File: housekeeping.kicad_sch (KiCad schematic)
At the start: 41 parts, among them U14 MC34063A, U15 MC34063A, U16 TPS54302

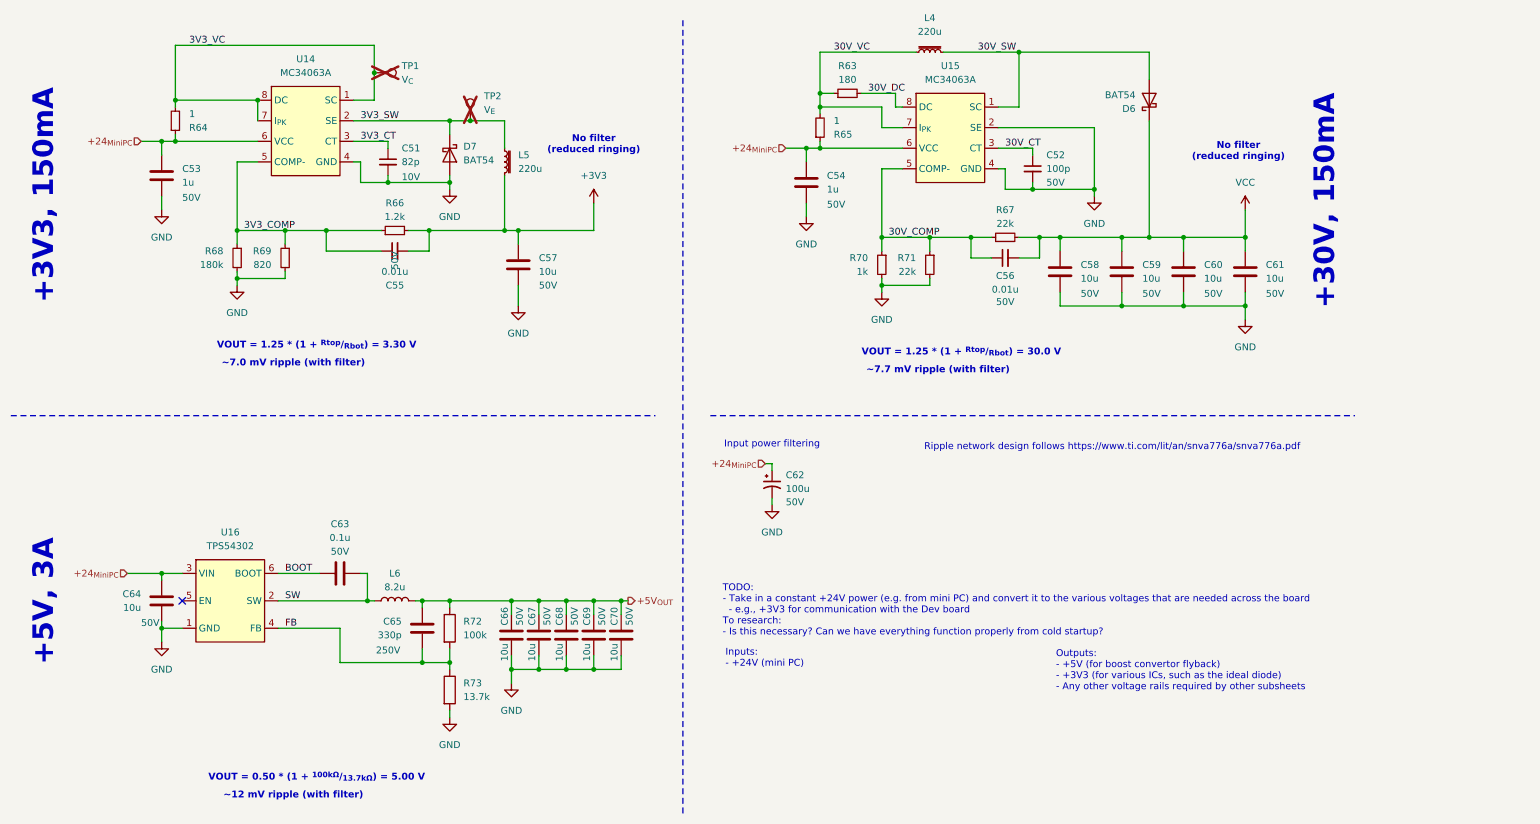
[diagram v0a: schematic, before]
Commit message: Add test points to all subsheets
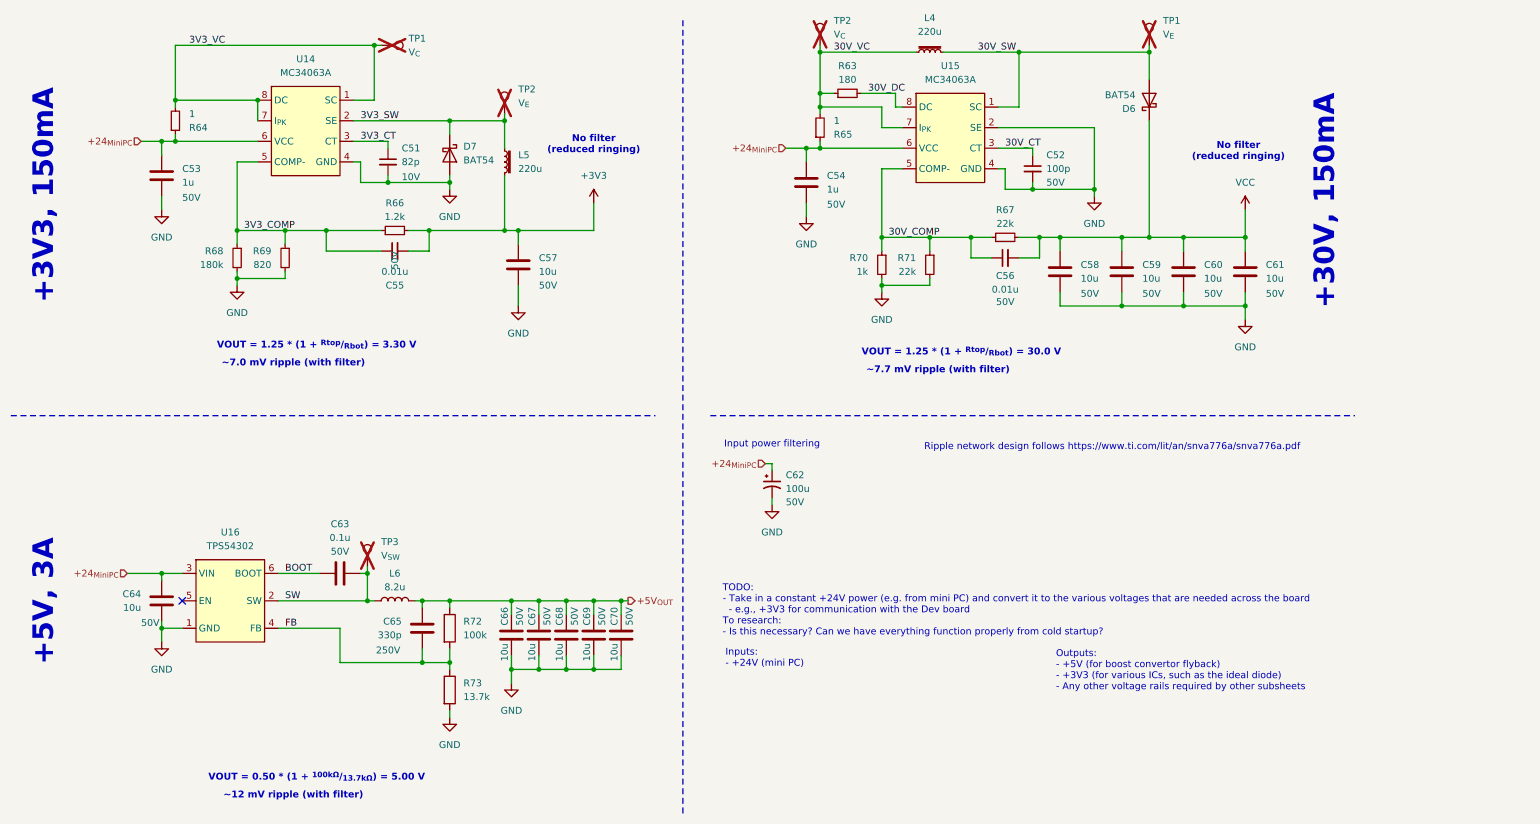
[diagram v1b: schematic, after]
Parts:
- added TP1: V_{E}, TestPoint:TestPoint_Bridge_Pitch2.0mm_Drill0.7mm, symbol Connector:TestPoint
- added TP2: V_{C}, TestPoint:TestPoint_Bridge_Pitch2.0mm_Drill0.7mm, symbol Connector:TestPoint
- added TP3: V_{SW}, TestPoint:TestPoint_Bridge_Pitch2.0mm_Drill0.7mm, symbol Connector:TestPoint
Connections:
- net 30V_SW: now also TP1.1
- net 30V_VC: now also TP2.1
- net SW: now also TP3.1
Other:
- moved on the sheet: TP1, TP2

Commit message: Renumbered components for rev 1b layout
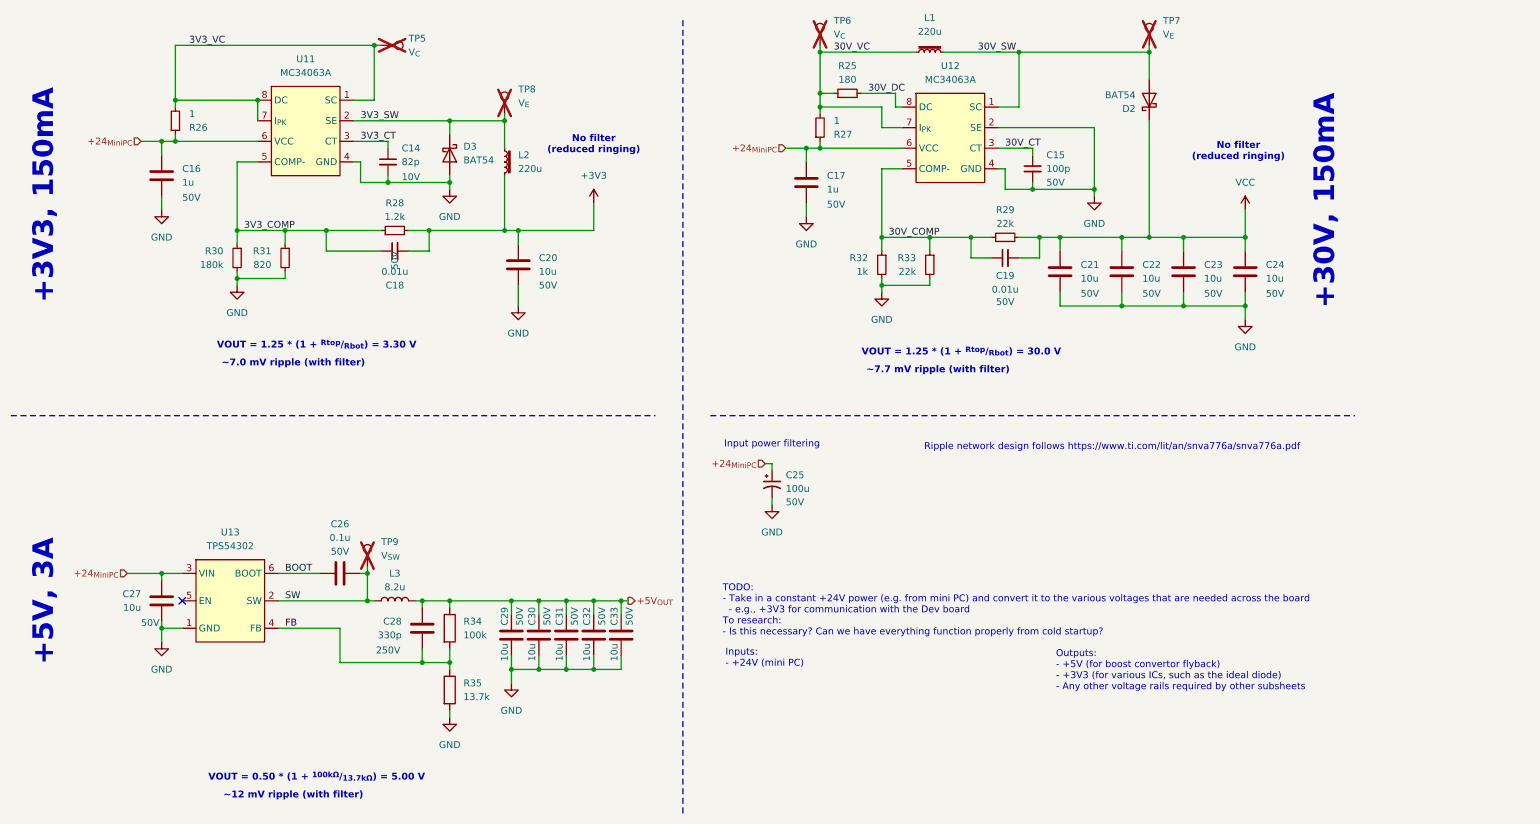
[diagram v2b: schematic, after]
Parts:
- renumbered C51 to C14, C52 to C15, C53 to C16, C54 to C17, C55 to C18, C56 to C19, C57 to C20, C58 to C21, C59 to C22, C60 to C23, C61 to C24, C62 to C25, C63 to C26, C64 to C27, C65 to C28, C66 to C29, C67 to C30, C68 to C31, C69 to C32, C70 to C33, D6 to D2, D7 to D3, L4 to L1, L5 to L2, L6 to L3, R63 to R25, R64 to R26, R65 to R27, R66 to R28, R67 to R29, R68 to R30, R69 to R31, R70 to R32, R71 to R33, R72 to R34, R73 to R35, TP1 to TP5, TP2 to TP6, TP1 to TP7, TP2 to TP8, TP3 to TP9, U14 to U11, U15 to U12, U16 to U13

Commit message: Begin layout
Completed ideal diode layout
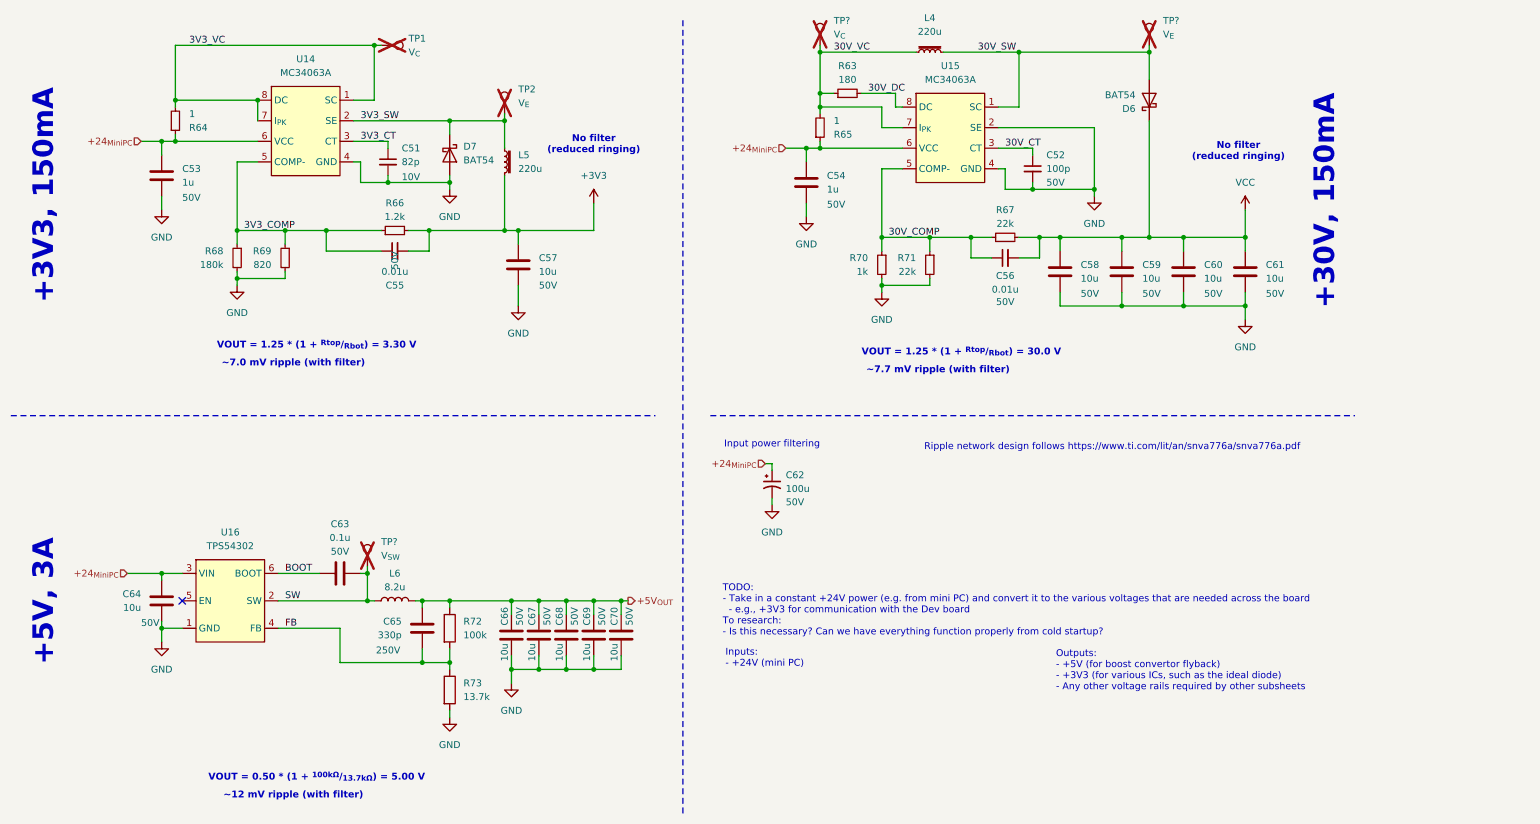
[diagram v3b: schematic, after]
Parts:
- renumbered C14 to C51, C15 to C52, C16 to C53, C17 to C54, C18 to C55, C19 to C56, C20 to C57, C21 to C58, C22 to C59, C23 to C60, C24 to C61, C25 to C62, C26 to C63, C27 to C64, C28 to C65, C29 to C66, C30 to C67, C31 to C68, C32 to C69, C33 to C70, D2 to D6, D3 to D7, L1 to L4, L2 to L5, L3 to L6, R25 to R63, R26 to R64, R27 to R65, R28 to R66, R29 to R67, R30 to R68, R31 to R69, R32 to R70, R33 to R71, R34 to R72, R35 to R73, TP5 to TP1, TP8 to TP2, TP7 to TP?, TP6 to TP?, TP9 to TP?, U11 to U14, U12 to U15, U13 to U16
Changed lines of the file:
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@@
 		(dnp no)
 		(fields_autoplaced yes)
-		(property "Reference" "#PWR093"
+		(property "Reference" "#PWR096"
 			(at 104.14 167.64 0)
 			(effects
@@
 		(dnp no)
 		(fields_autoplaced yes)
-		(property "Reference" "#PWR082"
+		(property "Reference" "#PWR085"
 			(at 130.81 69.85 0)
 			(effects
@@
 		(on_board yes)
 		(dnp no)
-		(property "Reference" "R28"
+		(property "Reference" "R66"
 			(at 93.98 66.04 90)
 			(effects
@@
 		(on_board yes)
 		(dnp no)
-		(property "Reference" "C23"
+		(property "Reference" "C60"
 			(at 243.84 77.4699 0)
 			(effects
@@
 		(on_board yes)
 		(dnp no)
-		(property "Reference" "D2"
+		(property "Reference" "D6"
 			(at 231.14 48.5776 90)
 			(effects
@@
 		(dnp no)
 		(fields_autoplaced yes)
-		(property "Reference" "#PWR087"
+		(property "Reference" "#PWR090"
 			(at 184.15 88.9 0)
 			(effects
@@
 		(dnp no)
 		(fields_autoplaced yes)
-		(property "Reference" "L3"
+		(property "Reference" "L6"
 			(at 93.98 134.62 90)
 			(effects
@@
 		(dnp no)
 		(fields_autoplaced yes)
-		(property "Reference" "#PWR088"
+		(property "Reference" "#PWR091"
 			(at 116.84 91.44 0)
 			(effects
@@
 		(on_board yes)
 		(dnp no)
-		(property "Reference" "C24"
+		(property "Reference" "C61"
 			(at 255.27 77.4699 0)
 			(effects
@@
 		(dnp yes)
 		(fields_autoplaced yes)
-		(property "Reference" "TP7"
+		(property "Reference" "TP?"
 			(at 236.22 32.2579 0)
 			(effects
@@
 		)
 		(instances
+			(project "SupercapManager"
+				(path "/6197145b-e7d4-44cc-9d90-537b6501bf60/2b4de7d2-e111-42d9-afee-f810f96a2f61"
+					(reference "TP?")
+					(unit 1)
+				)
+			)
 			(project "Rev 1B"
 				(path "/e5f99deb-ef42-4c5f-b80a-388477910e20/1e0b2151-e075-4f05-b22a-12d6722ef31a"
@@
 		(dnp no)
 		(fields_autoplaced yes)
-		(property "Reference" "R35"
+		(property "Reference" "R73"
 			(at 106.68 154.9399 0)
 			(effects
@@
 		(on_board yes)
 		(dnp no)
-		(property "Reference" "R26"
+		(property "Reference" "R64"
 			(at 55.88 52.0701 0)
 			(effects
@@
 		(on_board yes)
 		(dnp no)
-		(property "Reference" "C33"
+		(property "Reference" "C70"
 			(at 134.62 144.272 90)
 			(effects
@@
 		(dnp yes)
 		(fields_autoplaced yes)
-		(property "Reference" "TP6"
+		(property "Reference" "TP?"
 			(at 175.26 32.2579 0)
 			(effects
@@
 		)
 		(instances
+			(project "SupercapManager"
+				(path "/6197145b-e7d4-44cc-9d90-537b6501bf60/2b4de7d2-e111-42d9-afee-f810f96a2f61"
+					(reference "TP?")
+					(unit 1)
+				)
+			)
 			(project "Rev 1B"
 				(path "/e5f99deb-ef42-4c5f-b80a-388477910e20/1e0b2151-e075-4f05-b22a-12d6722ef31a"
@@
 		(on_board yes)
 		(dnp no)
-		(property "Reference" "C25"
+		(property "Reference" "C62"
 			(at 166.37 116.4081 0)
 			(effects
@@
 		(dnp no)
 		(fields_autoplaced yes)
-		(property "Reference" "#PWR091"
+		(property "Reference" "#PWR094"
 			(at 50.8 153.67 0)
 			(effects
@@
 		(on_board yes)
 		(dnp no)
-		(property "Reference" "C32"
+		(property "Reference" "C69"
 			(at 129.54 144.272 90)
 			(effects
@@
 		(on_board yes)
 		(dnp no)
-		(property "Reference" "C19"
+		(property "Reference" "C56"
 			(at 207.01 79.502 90)
 			(effects
@@
 		(dnp no)
 		(fields_autoplaced yes)
-		(property "Reference" "#PWR081"
+		(property "Reference" "#PWR084"
 			(at 223.52 71.12 0)
 			(effects
@@
 		(dnp no)
 		(fields_autoplaced yes)
-		(property "Reference" "R34"
+		(property "Reference" "R72"
 			(at 106.68 143.5099 0)
 			(effects
@@
 		(dnp no)
 		(fields_autoplaced yes)
-		(property "Reference" "U12"
+		(property "Reference" "U15"
 			(at 196.85 40.64 0)
 			(effects
@@
 		(dnp yes)
 		(fields_autoplaced yes)
-		(property "Reference" "TP5"
+		(property "Reference" "TP1"
 			(at 96.52 35.5599 90)
 			(effects
@@
 		(on_board yes)
 		(dnp no)
-		(property "Reference" "R29"
+		(property "Reference" "R67"
 			(at 207.01 67.31 90)
 			(effects
@@
 		(on_board yes)
 		(dnp no)
-		(property "Reference" "D3"
+		(property "Reference" "D7"
 			(at 106.68 55.5624 90)
 			(effects
@@
 		(dnp no)
 		(fields_autoplaced yes)
-		(property "Reference" "#PWR089"
+		(property "Reference" "#PWR092"
 			(at 251.46 93.98 0)
 			(effects
@@
 		(dnp no)
 		(fields_autoplaced yes)
-		(property "Reference" "#PWR092"
+		(property "Reference" "#PWR095"
 			(at 115.57 161.29 0)
 			(effects
@@
 		(on_board yes)
 		(dnp no)
-		(property "Reference" "C14"
+		(property "Reference" "C51"
 			(at 95.25 55.88 0)
 			(effects
@@
 		(on_board yes)
 		(dnp no)
-		(property "Reference" "C29"
+		(property "Reference" "C66"
 			(at 114.3 144.272 90)
 			(effects
@@
 		(dnp no)
 		(fields_autoplaced yes)
-		(property "Reference" "#PWR085"
+		(property "Reference" "#PWR088"
 			(at 170.18 74.93 0)
 			(effects
@@
 		(dnp no)
 		(fields_autoplaced yes)
-		(property "Reference" "#PWR090"
+		(property "Reference" "#PWR093"
 			(at 163.83 128.27 0)
 			(effects
@@
 		(on_board yes)
 		(dnp no)
-		(property "Reference" "R25"
+		(property "Reference" "R63"
 			(at 177.8 40.64 90)
 			(effects
@@
 		(dnp no)
 		(fields_autoplaced yes)
-		(property "Reference" "#PWR080"
+		(property "Reference" "#PWR083"
 			(at 104.14 69.85 0)
 			(effects
@@
 		(on_board yes)
 		(dnp no)
-		(property "Reference" "R31"
+		(property "Reference" "R69"
 			(at 71.12 74.9299 0)
 			(effects
@@
 		(on_board yes)
 		(dnp no)
-		(property "Reference" "C21"
+		(property "Reference" "C58"
 			(at 220.98 77.4699 0)
 			(effects
@@
 		(on_board yes)
 		(dnp no)
-		(property "Reference" "C22"
+		(property "Reference" "C59"
 			(at 232.41 77.4699 0)
 			(effects
@@
 		(dnp no)
 		(fields_autoplaced yes)
-		(property "Reference" "L1"
+		(property "Reference" "L4"
 			(at 193.04 31.75 90)
 			(effects
@@
 		(dnp no)
 		(fields_autoplaced yes)
-		(property "Reference" "#PWR086"
+		(property "Reference" "#PWR089"
 			(at 64.77 87.63 0)
 			(effects
@@
 		(dnp no)
 		(fields_autoplaced yes)
-		(property "Reference" "U11"
+		(property "Reference" "U14"
 			(at 77.47 39.37 0)
 			(effects
@@
 		(on_board yes)
 		(dnp no)
-		(property "Reference" "R27"
+		(property "Reference" "R65"
 			(at 175.26 53.3401 0)
 			(effects
@@
 		(dnp no)
 		(fields_autoplaced yes)
-		(property "Reference" "#PWR084"
+		(property "Reference" "#PWR087"
 			(at 251.46 71.12 0)
 			(effects
@@
 		(on_board yes)
 		(dnp no)
-		(property "Reference" "C27"
+		(property "Reference" "C64"
 			(at 46.99 138.4299 0)
 			(effects
@@
 		(on_board yes)
 		(dnp no)
-		(property "Reference" "C20"
+		(property "Reference" "C57"
 			(at 120.65 76.1999 0)
 			(effects
@@
 		(on_board yes)
 		(dnp no)
-		(property "Reference" "C28"
+		(property "Reference" "C65"
 			(at 95.25 143.5099 0)
 			(effects
@@
 		(on_board yes)
 		(dnp no)
-		(property "Reference" "C17"
+		(property "Reference" "C54"
 			(at 173.99 60.9599 0)
 			(effects
@@
 		(on_board yes)
 		(dnp no)
-		(property "Reference" "C26"
+		(property "Reference" "C63"
 			(at 83.82 125.476 90)
 			(effects
@@
 		(on_board yes)
 		(dnp no)
-		(property "Reference" "C31"
+		(property "Reference" "C68"
 			(at 124.46 144.272 90)
 			(effects
@@
 		(dnp no)
 		(fields_autoplaced yes)
-		(property "Reference" "L2"
+		(property "Reference" "L5"
 			(at 116.84 57.1499 0)
 			(effects
@@
 		(dnp no)
 		(fields_autoplaced yes)
-		(property "Reference" "U13"
+		(property "Reference" "U16"
 			(at 63.5 127 0)
 			(effects
@@
 		(on_board yes)
 		(dnp no)
-		(property "Reference" "R33"
+		(property "Reference" "R71"
 			(at 190.5 76.1999 0)
 			(effects
@@
 		(dnp no)
 		(fields_autoplaced yes)
-		(property "Reference" "#PWR083"
+		(property "Reference" "#PWR086"
 			(at 50.8 73.66 0)
 			(effects
@@
 		(on_board yes)
 		(dnp no)
-		(property "Reference" "R30"
+		(property "Reference" "R68"
 			(at 62.23 74.9299 0)
 			(effects
@@
 		(on_board yes)
 		(dnp no)
-		(property "Reference" "C30"
+		(property "Reference" "C67"
 			(at 119.38 144.272 90)
 			(effects
@@
 		(on_board yes)
 		(dnp no)
-		(property "Reference" "R32"
+		(property "Reference" "R70"
 			(at 181.61 76.1999 0)
 			(effects
@@
 		(on_board yes)
 		(dnp no)
-		(property "Reference" "C18"
+		(property "Reference" "C55"
 			(at 93.9863 81.28 90)
 			(effects
@@
 		(dnp yes)
 		(fields_autoplaced yes)
-		(property "Reference" "TP9"
+		(property "Reference" "TP?"
 			(at 91.44 128.7779 0)
 			(effects
@@
 		)
 		(instances
+			(project "SupercapManager"
+				(path "/6197145b-e7d4-44cc-9d90-537b6501bf60/2b4de7d2-e111-42d9-afee-f810f96a2f61"
+					(reference "TP?")
+					(unit 1)
+				)
+			)
 			(project "Rev 1B"
 				(path "/e5f99deb-ef42-4c5f-b80a-388477910e20/1e0b2151-e075-4f05-b22a-12d6722ef31a"
@@
 		(on_board yes)
 		(dnp no)
-		(property "Reference" "C16"
+		(property "Reference" "C53"
 			(at 54.61 59.6899 0)
 			(effects
@@
 		(on_board yes)
 		(dnp no)
-		(property "Reference" "C15"
+		(property "Reference" "C52"
 			(at 214.63 57.15 0)
 			(effects
@@
 		(dnp yes)
 		(fields_autoplaced yes)
-		(property "Reference" "TP8"
+		(property "Reference" "TP2"
 			(at 116.84 44.9579 0)
 			(effects
